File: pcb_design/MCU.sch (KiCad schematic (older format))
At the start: 15 parts, among them P2 SWD, U1 STM32F40X_LQFP64, X2 8MHz 10ppm

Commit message: Updated MCU sheet to comply with VESC 6 pinout. Added 5v analog inputs and updated some labels
Signed-off-by: Marcos Chaparro <mchaparro@paltatech.com>
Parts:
- removed C10, C11, C12, C13, C14, C16, C17, C31, C35: 2.2u, CRF1:SMD-0603_c, symbol C-RESCUE-BLDC_4
- removed C15, C38: 15p, CRF1:SMD-0603_c, symbol C-RESCUE-BLDC_4
- removed C32: 100n, CRF1:SMD-0603_c, symbol C-RESCUE-BLDC_4
- removed P2: SWD, CRF1:MICRO_JST_6, symbol CONN_6
- removed X2: 8MHz 10ppm, CRF1:Crystal_5x3mm, symbol CRYSTAL_SMD
- added C10, C11, C12, C3, C4, C5, C6, C9: 2.2u, IPC7351-Nominal:CAPC1608X55, symbol C
- added C2, C8: 15p, IPC7351-Nominal:CAPC1608X55, symbol C
- added C7: 100n, IPC7351-Nominal:CAPC1608X55, symbol C
- added X?: ABM3B - 8MHz, IPC7351-Nominal:OSCCC320X500X150, symbol XTAL-ABRACON-ABM3B
- U1: footprint CRF1:lqfp64_pad_mod -> Housings_QFP:LQFP-64_10x10mm_Pitch0.5mm
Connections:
- net labels added: ADC_15, I_phase_U, I_phase_V, I_phase_W, PB12, PB3, PB4, PD2, PWM_AUX, PWM_UB, PWM_UT, PWM_VB, PWM_VT, PWM_WB, PWM_WT, RX_SDA_NSS, SPI3_CS, SPI3_MISO, SPI3_MOSI, SPI3_SCK, TX_SCL_MOSI, V_phase_U, V_phase_V, V_phase_W, ~DRIVER_RESET, ~FAULT
- net labels removed: BR_SO1, BR_SO2, DC_CAL, EN_GATE, FAULT, H1, H2, H3, L1, L2, L3, RX_SCL_MOSI, SENS1, SENS2, SENS3, SERVO, TX_SDA_NSS
- wire segments 60 -> 73
- no-connect marks 13 -> 5
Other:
- note removed: "Programming / Debug\nconnector"
- note removed: "Required for USB\nto work"
- note removed: "Reset pin internally\npulled up"

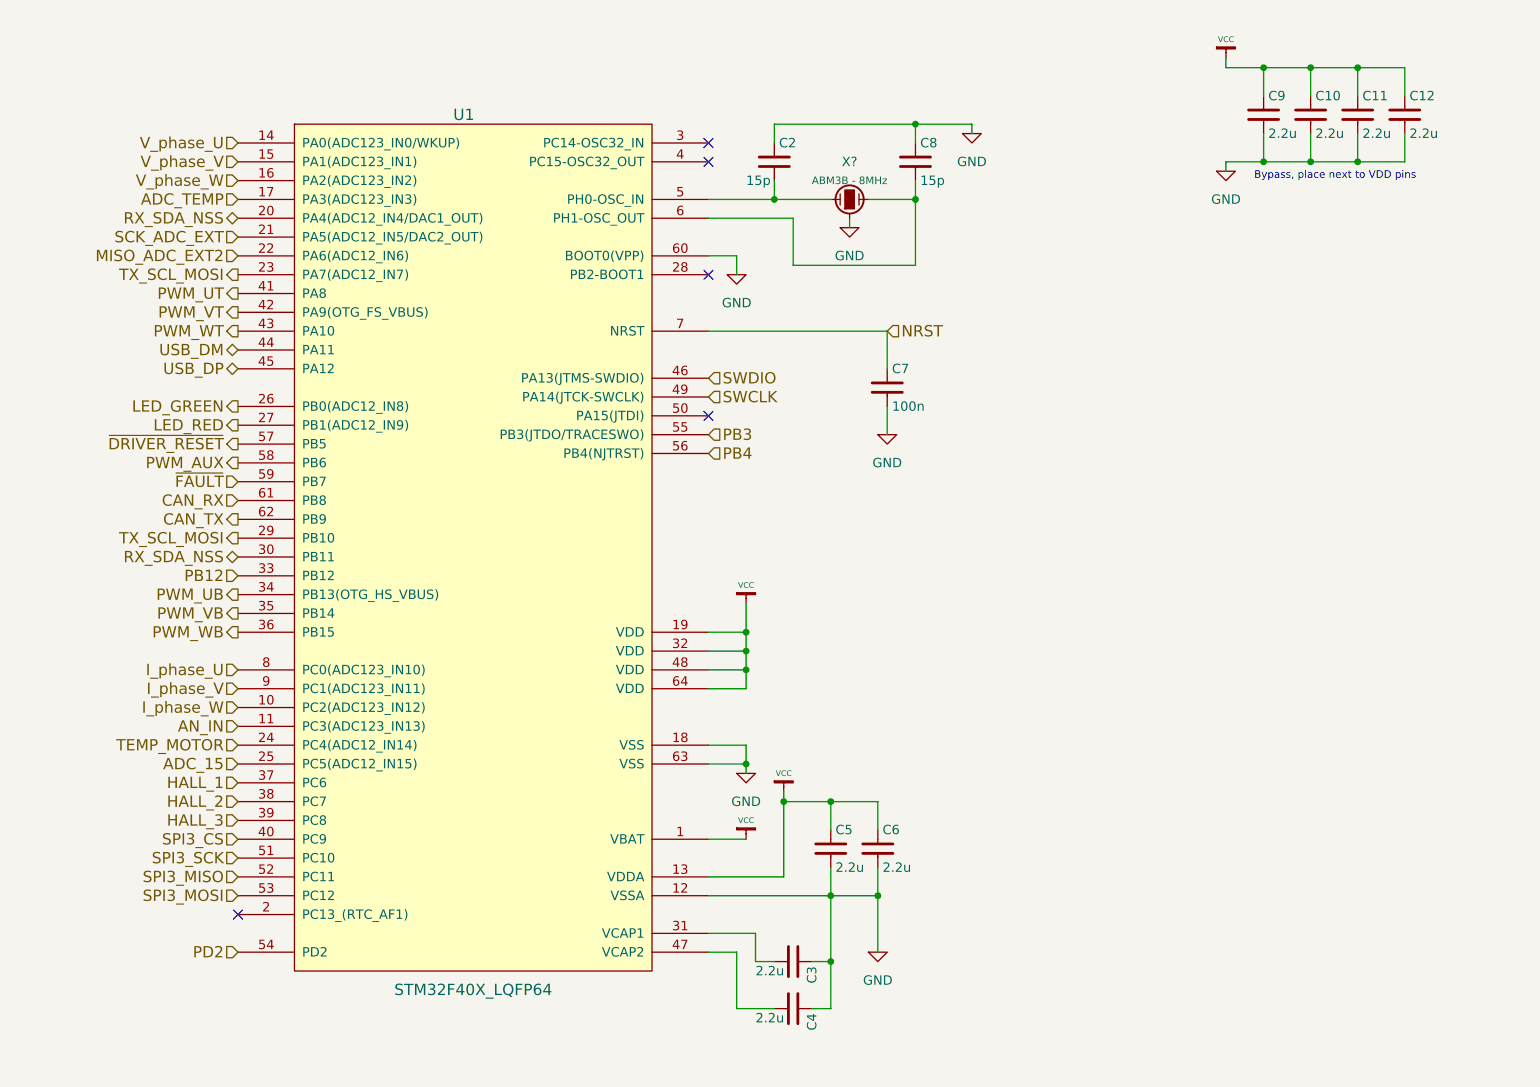
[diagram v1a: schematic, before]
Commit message: Components placement, 3D models, updated some footprints to nominal IPC type
Signed-off-by: Marcos Chaparro <mchaparro@paltatech.com>
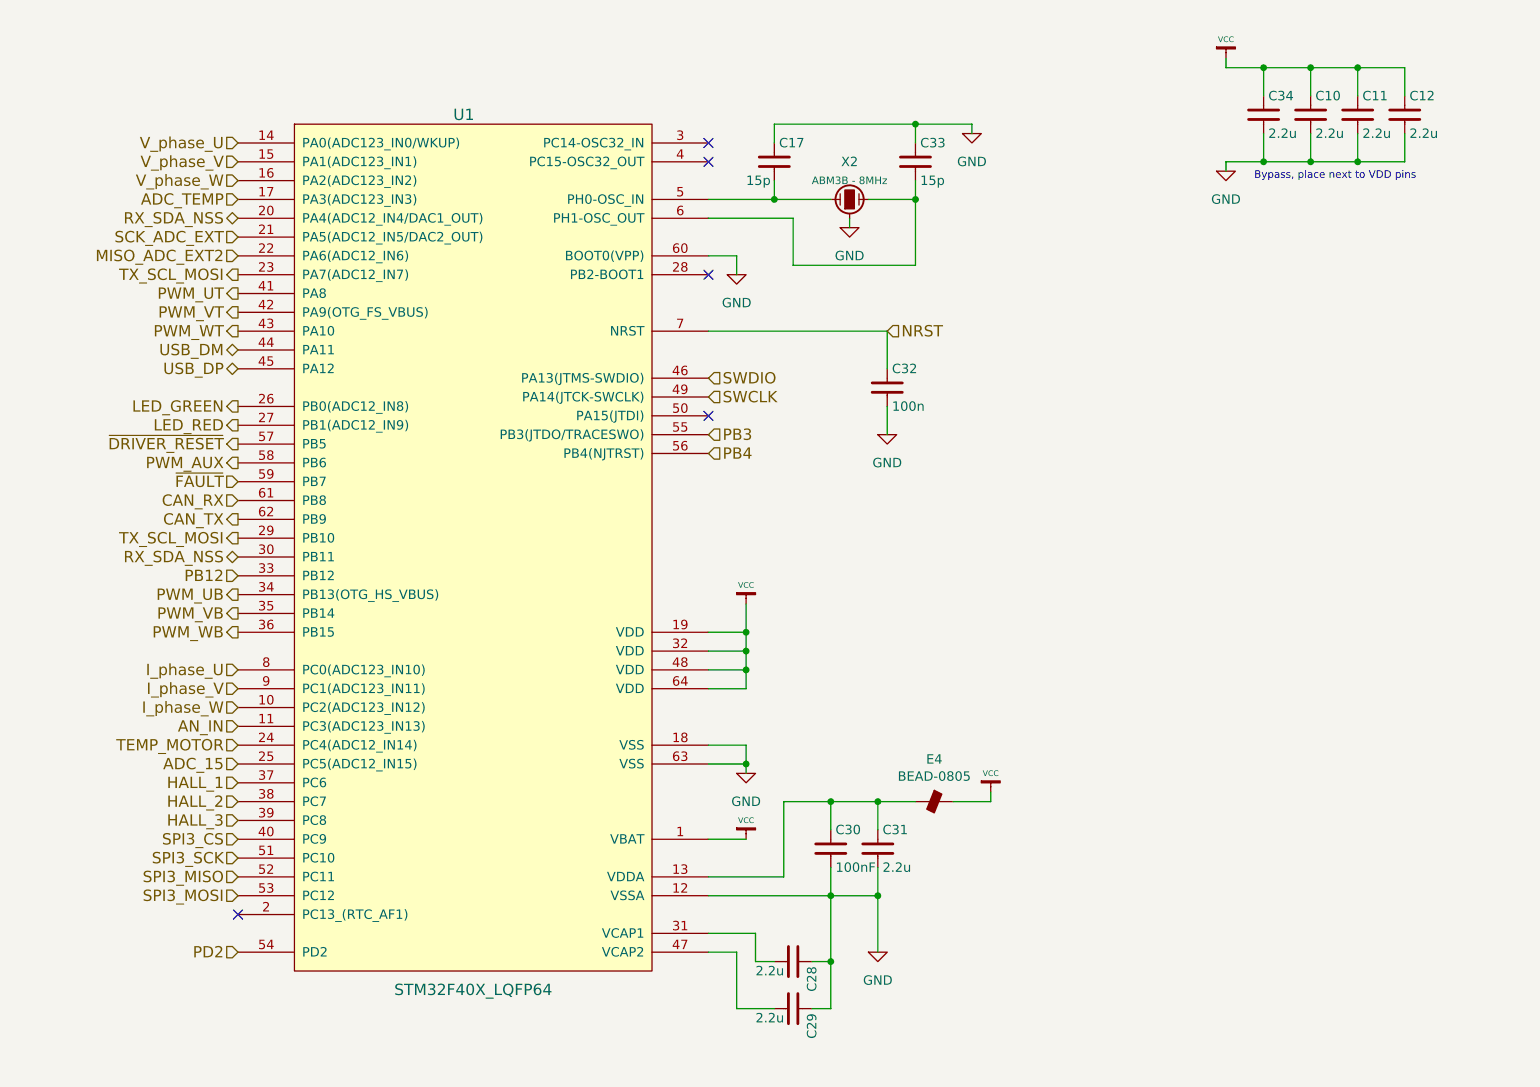
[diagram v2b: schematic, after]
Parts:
- added E4: BEAD-0805, IPC7351-Nominal:INDC2012X130, symbol BEAD-0805
- C30: renamed from C5; value 2.2u -> 100nF
- U1: footprint Housings_QFP:LQFP-64_10x10mm_Pitch0.5mm -> IPC7351-Nominal:QFP50P1200X1200X100-64
- gave numbers to parts that had none: 1
- renumbered C2 to C17, C3 to C28, C4 to C29, C6 to C31, C7 to C32, C8 to C33, C9 to C34
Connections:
- net VCC: now also E4.2; no longer C30.1, C31.1, U1.13 (VDDA)
- new net: C30.1, C31.1, E4.1, U1.13 (VDDA)
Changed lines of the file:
@@
 RX_SDA_NSS
 $Comp
-L VCC #PWR028
+L VCC #PWR106
 U 1 1 572D84D8
-P 6550 4950
-F 0 "#PWR028" H 6550 5050 30  0001 C CNN
-F 1 "VCC" H 6550 5050 30  0000 C CNN
-F 2 "" H 6550 4950 60  0001 C CNN
-F 3 "" H 6550 4950 60  0001 C CNN
-	1    6550 4950
-	1    0    0    -1
-$EndComp
-$Comp
-L VCC #PWR029
+P 7650 4950
+F 0 "#PWR106" H 7650 5050 30  0001 C CNN
+F 1 "VCC" H 7650 5050 30  0000 C CNN
+F 2 "" H 7650 4950 60  0001 C CNN
+F 3 "" H 7650 4950 60  0001 C CNN
+	1    7650 4950
+	1    0    0    -1
+$EndComp
+$Comp
+L VCC #PWR99
 U 1 1 572D84D9
 P 6350 3950
-F 0 "#PWR029" H 6350 4050 30  0001 C CNN
+F 0 "#PWR99" H 6350 4050 30  0001 C CNN
 F 1 "VCC" H 6350 4050 30  0000 C CNN
 F 2 "" H 6350 3950 60  0001 C CNN
@@
 NoConn ~ 6150 2200
 $Comp
-L VCC #PWR030
+L VCC #PWR101
 U 1 1 572D84DA
 P 6350 5200
-F 0 "#PWR030" H 6350 5300 30  0001 C CNN
+F 0 "#PWR101" H 6350 5300 30  0001 C CNN
 F 1 "VCC" H 6350 5300 30  0000 C CNN
 F 2 "" H 6350 5200 60  0001 C CNN
@@
 Wire Wire Line
 	7050 5000 7050 5150
-Connection ~ 6550 5000
-Wire Wire Line
-	6550 5000 6800 5000
-Wire Wire Line
-	6800 5000 7050 5000
+Wire Wire Line
+	6550 5000 7250 5000
 Wire Wire Line
 	6800 5150 6800 5000
@@
 	6550 5400 6150 5400
 Wire Wire Line
-	6350 3950 6350 4100
-Wire Wire Line
-	6350 4100 6350 4200
-Wire Wire Line
-	6350 4200 6350 4300
-Wire Wire Line
-	6350 4300 6350 4400
+	6350 3950 6350 4400
 Wire Wire Line
 	6300 2100 6300 2200
@@
 	7250 1400 7250 1500
 Wire Wire Line
-	6500 1400 7250 1400
-Wire Wire Line
-	7250 1400 7550 1400
+	6500 1400 7550 1400
 Wire Wire Line
 	6500 1400 6500 1500
@@
 	7000 1800 7250 1800
 Wire Wire Line
-	7250 1700 7250 1800
-Wire Wire Line
-	7250 1800 7250 2150
+	7250 1700 7250 2150
 Wire Wire Line
 	6600 2150 6600 1900
@@
 	6600 1900 6150 1900
 Wire Wire Line
-	6150 1800 6500 1800
-Wire Wire Line
-	6500 1800 6800 1800
+	6150 1800 6800 1800
 Connection ~ 6350 4100
 Wire Wire Line
@@
 	6150 4700 6350 4700
 Wire Wire Line
-	6350 4700 6350 4800
-Wire Wire Line
-	6350 4800 6350 4850
-Wire Wire Line
-	6550 4950 6550 5000
+	6350 4700 6350 4850
 Wire Wire Line
 	6550 5000 6550 5400
 Connection ~ 6800 5500
 Wire Wire Line
-	7050 5350 7050 5500
-Wire Wire Line
-	7050 5500 7050 5800
+	7050 5350 7050 5800
 Wire Wire Line
 	6300 6100 6500 6100
@@
 Connection ~ 6800 5850
 Wire Wire Line
-	6150 5500 6800 5500
-Wire Wire Line
-	6800 5500 7050 5500
-Wire Wire Line
-	6800 5350 6800 5500
-Wire Wire Line
-	6800 5500 6800 5850
-Wire Wire Line
-	6800 5850 6800 6100
+	6150 5500 7050 5500
+Wire Wire Line
+	6800 5350 6800 6100
 Wire Wire Line
 	6800 5850 6700 5850
@@
 	6800 6100 6700 6100
 $Comp
-L VCC #PWR031
+L VCC #PWR107
 U 1 1 572D84DB
 P 8900 1050
-F 0 "#PWR031" H 8900 1150 30  0001 C CNN
+F 0 "#PWR107" H 8900 1150 30  0001 C CNN
 F 1 "VCC" H 8900 1150 30  0000 C CNN
 F 2 "" H 8900 1050 60  0001 C CNN
@@
 	9850 1100 9850 1250
 Wire Wire Line
-	8900 1100 9100 1100
-Wire Wire Line
-	9100 1100 9350 1100
-Wire Wire Line
-	9350 1100 9600 1100
-Wire Wire Line
-	9600 1100 9850 1100
+	8900 1100 9850 1100
 Wire Wire Line
 	8900 1050 8900 1100
@@
 	9850 1600 9850 1450
 Wire Wire Line
-	8900 1600 9100 1600
-Wire Wire Line
-	9100 1600 9350 1600
-Wire Wire Line
-	9350 1600 9600 1600
-Wire Wire Line
-	9600 1600 9850 1600
+	8900 1600 9850 1600
 Wire Wire Line
 	8900 1650 8900 1600
@@
 Bypass, place next to VDD pins
 $Comp
-L GND #PWR032
+L GND #PWR105
 U 1 1 572D84DC
 P 7550 1450
-F 0 "#PWR032" H 7550 1200 50  0001 C CNN
+F 0 "#PWR105" H 7550 1200 50  0001 C CNN
 F 1 "GND" H 7550 1300 50  0000 C CNN
 F 2 "" H 7550 1450 60  0000 C CNN
@@
 $EndComp
 $Comp
-L C C2
+L C C17
 U 1 1 572D84DD
 P 6500 1600
-F 0 "C2" H 6525 1700 50  0000 L CNN
+F 0 "C17" H 6525 1700 50  0000 L CNN
 F 1 "15p" H 6350 1500 50  0000 L CNN
 F 2 "IPC7351-Nominal:CAPC1608X55" H 6538 1450 30  0001 C CNN
@@
 $EndComp
 $Comp
-L C C8
+L C C33
 U 1 1 572D84DE
 P 7250 1600
-F 0 "C8" H 7275 1700 50  0000 L CNN
+F 0 "C33" H 7275 1700 50  0000 L CNN
 F 1 "15p" H 7275 1500 50  0000 L CNN
 F 2 "IPC7351-Nominal:CAPC1608X55" H 7288 1450 30  0001 C CNN
@@
 $EndComp
 $Comp
-L GND #PWR033
+L GND #PWR102
 U 1 1 572D84DF
 P 6900 1950
-F 0 "#PWR033" H 6900 1700 50  0001 C CNN
+F 0 "#PWR102" H 6900 1700 50  0001 C CNN
 F 1 "GND" H 6900 1800 50  0000 C CNN
 F 2 "" H 6900 1950 60  0000 C CNN
@@
 $EndComp
 $Comp
-L GND #PWR034
+L GND #PWR98
 U 1 1 572D84E0
 P 6300 2200
-F 0 "#PWR034" H 6300 1950 50  0001 C CNN
+F 0 "#PWR98" H 6300 1950 50  0001 C CNN
 F 1 "GND" H 6300 2050 50  0000 C CNN
 F 2 "" H 6300 2200 60  0000 C CNN
@@
 	6900 1950 6900 1900
 $Comp
-L C C7
+L C C32
 U 1 1 572D84E1
 P 7100 2800
-F 0 "C7" H 7125 2900 50  0000 L CNN
+F 0 "C32" H 7125 2900 50  0000 L CNN
 F 1 "100n" H 7125 2700 50  0000 L CNN
 F 2 "IPC7351-Nominal:CAPC1608X55" H 7138 2650 30  0001 C CNN
@@
 $EndComp
 $Comp
-L GND #PWR035
+L GND #PWR104
 U 1 1 572D84E2
 P 7100 3050
-F 0 "#PWR035" H 7100 2800 50  0001 C CNN
+F 0 "#PWR104" H 7100 2800 50  0001 C CNN
 F 1 "GND" H 7100 2900 50  0000 C CNN
 F 2 "" H 7100 3050 60  0000 C CNN
@@
 SWCLK
 $Comp
-L GND #PWR036
+L GND #PWR103
 U 1 1 572D84E3
 P 7050 5800
-F 0 "#PWR036" H 7050 5550 50  0001 C CNN
+F 0 "#PWR103" H 7050 5550 50  0001 C CNN
 F 1 "GND" H 7050 5650 50  0000 C CNN
 F 2 "" H 7050 5800 60  0000 C CNN
@@
 $EndComp
 $Comp
-L GND #PWR037
+L GND #PWR100
 U 1 1 572D84E4
 P 6350 4850
-F 0 "#PWR037" H 6350 4600 50  0001 C CNN
+F 0 "#PWR100" H 6350 4600 50  0001 C CNN
 F 1 "GND" H 6350 4700 50  0000 C CNN
 F 2 "" H 6350 4850 60  0000 C CNN
@@
 $EndComp
 $Comp
-L C C5
+L C C30
 U 1 1 572D84E5
 P 6800 5250
-F 0 "C5" H 6825 5350 50  0000 L CNN
-F 1 "2.2u" H 6825 5150 50  0000 L CNN
+F 0 "C30" H 6825 5350 50  0000 L CNN
+F 1 "100nF" H 6825 5150 50  0000 L CNN
 F 2 "IPC7351-Nominal:CAPC1608X55" H 6838 5100 30  0001 C CNN
 F 3 "" H 6800 5250 60  0000 C CNN
@@
 $EndComp
 $Comp
-L C C6
+L C C31
 U 1 1 572D84E6
 P 7050 5250
-F 0 "C6" H 7075 5350 50  0000 L CNN
+F 0 "C31" H 7075 5350 50  0000 L CNN
 F 1 "2.2u" H 7075 5150 50  0000 L CNN
 F 2 "IPC7351-Nominal:CAPC1608X55" H 7088 5100 30  0001 C CNN
@@
 $EndComp
 $Comp
-L C C3
+L C C28
 U 1 1 572D84E7
 P 6600 5850
-F 0 "C3" H 6625 5950 50  0000 L CNN
+F 0 "C28" H 6625 5950 50  0000 L CNN
 F 1 "2.2u" V 6650 5650 50  0000 L CNN
 F 2 "IPC7351-Nominal:CAPC1608X55" H 6638 5700 30  0001 C CNN
@@
 $EndComp
 $Comp
-L C C4
+L C C29
 U 1 1 572D84E8
 P 6600 6100
-F 0 "C4" H 6625 6200 50  0000 L CNN
+F 0 "C29" H 6625 6200 50  0000 L CNN
 F 1 "2.2u" V 6650 5900 50  0000 L CNN
 F 2 "IPC7351-Nominal:CAPC1608X55" H 6638 5950 30  0001 C CNN
@@
 $EndComp
 $Comp
-L GND #PWR038
+L GND #PWR108
 U 1 1 572D84E9
 P 8900 1650
-F 0 "#PWR038" H 8900 1400 50  0001 C CNN
+F 0 "#PWR108" H 8900 1400 50  0001 C CNN
 F 1 "GND" H 8900 1500 50  0000 C CNN
 F 2 "" H 8900 1650 60  0000 C CNN
@@
 $EndComp
 $Comp
-L C C9
+L C C34
 U 1 1 572D84EA
 P 9100 1350
-F 0 "C9" H 9125 1450 50  0000 L CNN
+F 0 "C34" H 9125 1450 50  0000 L CNN
 F 1 "2.2u" H 9125 1250 50  0000 L CNN
 F 2 "IPC7351-Nominal:CAPC1608X55" H 9138 1200 30  0001 C CNN
@@
 F 0 "U1" H 4850 5950 60  0000 C CNN
 F 1 "STM32F40X_LQFP64" H 4900 1300 60  0000 C CNN
-F 2 "Housings_QFP:LQFP-64_10x10mm_Pitch0.5mm" H 4900 3650 60  0001 C CNN
+F 2 "IPC7351-Nominal:QFP50P1200X1200X100-64" H 4900 3650 60  0001 C CNN
 F 3 "" H 4900 3650 60  0000 C CNN
 	1    4900 3650
@@
 PB4
 $Comp
-L XTAL-ABRACON-ABM3B X?
+L XTAL-ABRACON-ABM3B X2
 U 1 1 588E380B
 P 6900 1800
-F 0 "X?" V 7100 1800 50  0000 C CNN
+F 0 "X2" V 7100 1800 50  0000 C CNN
 F 1 "ABM3B - 8MHz" V 7000 1800 40  0000 C CNN
 F 2 "IPC7351-Nominal:OSCCC320X500X150" H 6900 1650 60  0001 C CNN
@@
 	0    -1   -1   0
 $EndComp
+Connection ~ 7050 5000
+Wire Wire Line
+	7450 5000 7650 5000
+Wire Wire Line
+	7650 5000 7650 4950
+$Comp
+L BEAD-0805 E4
+U 1 1 588F431A
+P 7350 5000
+F 0 "E4" H 7350 5225 50  0000 C CNN
+F 1 "BEAD-0805" H 7350 5134 50  0000 C CNN
+F 2 "IPC7351-Nominal:INDC2012X130" H 7350 4900 50  0001 C CNN
+F 3 "" H 7350 5050 60  0000 C CNN
+F 4 "BEAD SMD 100 @0MHz 1A [0805]" H 7350 4800 60  0001 C CNN "BOM"
+	1    7350 5000
+	1    0    0    -1
+$EndComp
 $EndSCHEMATC
